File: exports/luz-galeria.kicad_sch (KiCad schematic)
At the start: 41 parts

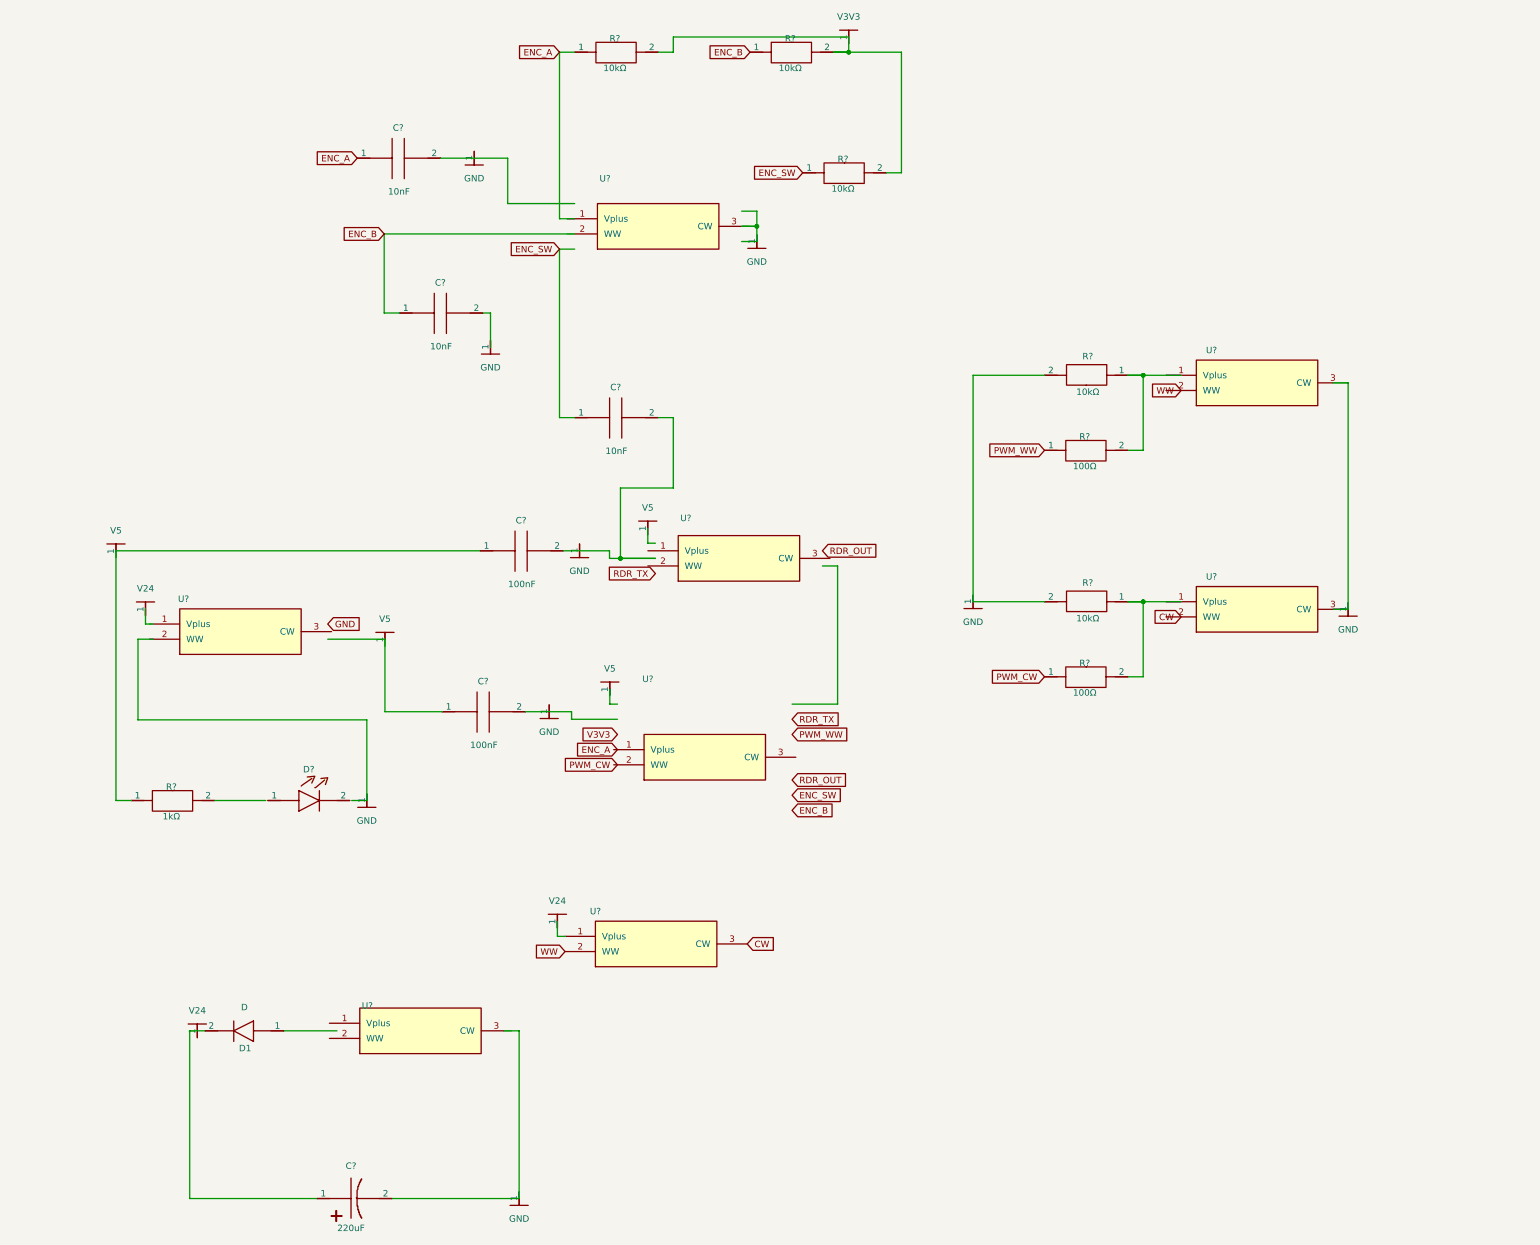
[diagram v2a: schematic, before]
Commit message: Re-layout: I/O on short edges, encoder flipped, full KiCad project export
Placement changes (App.tsx):
- Both terminals (J_IN/J_OUT) stacked on the LEFT short edge with screw
  openings facing -X (cables exit the same narrow side). Required rotating
  each terminal chip 270deg and relocating D1/C_BULK to the +X interior
  side of PowerInput.
- Encoder moved to the RIGHT short edge alone, so the knob is accessible
  without obstruction from the other components. Encoder support passives
  (RPU/C) moved to the -X interior side of EncoderInput.
- MosfetDriver shifted up; BuckRegulator nudged + its LED row tucked just
  below the MP1584 body to clear C_ESP (left) and the encoder pull-ups
  (right). Stitching vias re-placed.

Encoder cadModel flipped 180deg on X (rotationOffset) so the shaft renders
hanging DOWN, matching the upside-down install orientation visually.

Build passes routing-disabled DRC with 0 overlaps and 0 close-pad warnings.

KiCad export now uses --kicad-project + --kicad-project-zip:
- exports/luz-galeria-kicad.zip: full project (sch + pcb + pro), 120+
  symbols defined inline so it opens in KiCad 8/9 without missing symbols.
- Doc updated: recommended path is open the project in KiCad, then export
  a classic .net netlist for VeroRoute.
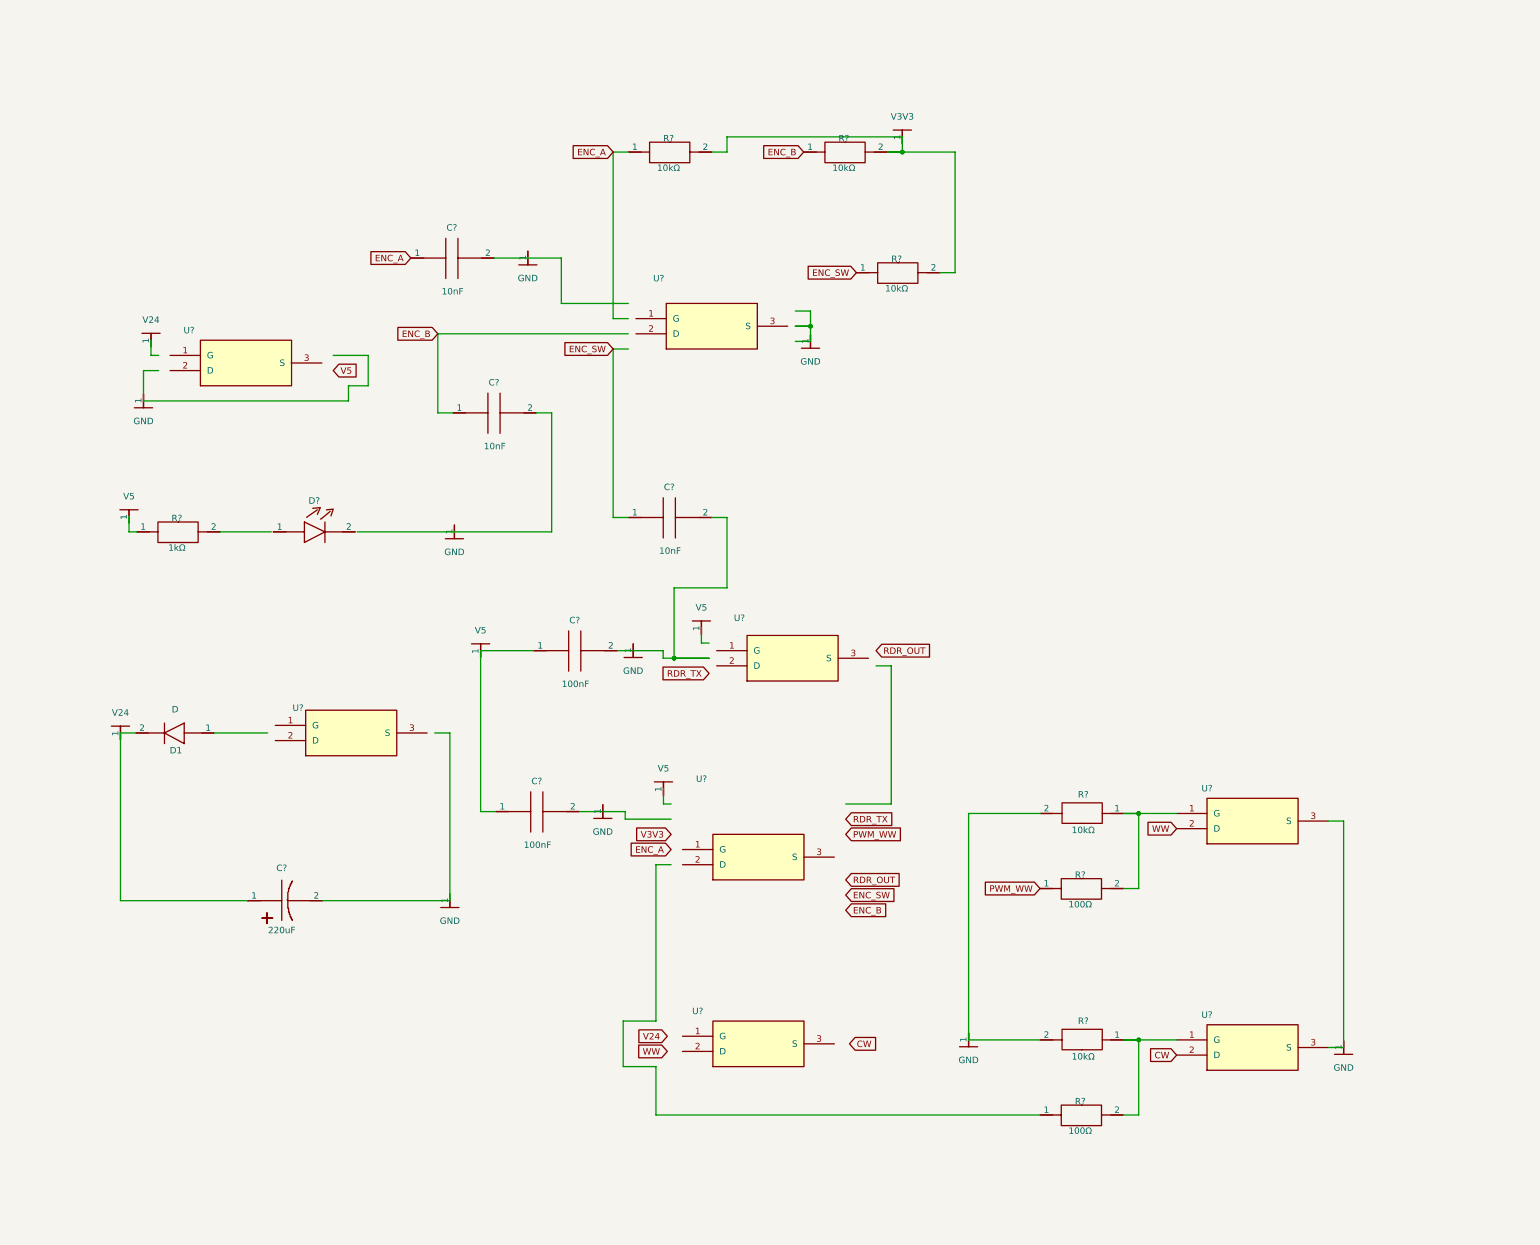
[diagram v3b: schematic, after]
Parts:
- removed C?: 220uF, symbol Device:capacitor_polarized_right
- removed C? (x3): 10nF, symbol Device:capacitor_right
- removed C? (x2): 100nF, symbol Device:capacitor_right
- removed D?: (no value), symbol Device:led_right
- removed GND (x9): GND, symbol Custom:rail_down
- removed R? (x2): 100Ω, symbol Device:boxresistor_right
- removed R? (x2): 10kΩ, symbol Device:boxresistor_left
- removed R? (x3): 10kΩ, symbol Device:boxresistor_right
- removed R?: 1kΩ, symbol Device:boxresistor_right
- removed U? (x8): (no value), symbol Device:U_chip
- removed V24 (x3): V24, symbol Custom:rail_up
- removed V5 (x4): V5, symbol Custom:rail_up
- added C? (x3): 10nF, symbol Device:capacitor_right
- added C? (x2): 100nF, symbol Device:capacitor_right
- added C?: 220uF, symbol Device:capacitor_polarized_right
- added D?: (no value), symbol Device:led_right
- added GND (x9): GND, symbol Custom:rail_down
- added R? (x3): 10kΩ, symbol Device:boxresistor_right
- added R? (x2): 10kΩ, symbol Device:boxresistor_left
- added R? (x2): 100Ω, symbol Device:boxresistor_right
- added R?: 1kΩ, symbol Device:boxresistor_right
- added U? (x8): (no value), symbol Device:U_chip
- added V24 (x2): V24, symbol Custom:rail_up
- added V5 (x4): V5, symbol Custom:rail_up
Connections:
- net CW: now also U?.2 (D)
- net ENC_A: now also C?.1, R?.1
- net ENC_B: now also C?.1, R?.1
- net ENC_SW: now also C?.1, R?.1
- net PWM_WW: now also R?.1
- net WW: now also U?.2 (D)
- net at D1.2: now also C?.2 (1)
- new net: R?.2, R?.2, R?.2
- new net: R?.1, R?.2, U?.1 (G) (x2)
- new net: U?.3 (S), U?.3 (S)
- new net: C?.1, C?.1
- new net: R?.2, R?.2
- new net: C?.2, C?.2
